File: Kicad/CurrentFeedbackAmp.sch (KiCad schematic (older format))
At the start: 97 parts, among them J1 Vin, J10 Protecc_Sup_In1, J11 Protecc_Inf_In1, J12 Protecc_Sup_In2, J13 Vdd, J14 Vcc, J15 Masa Filtros, J16 Masa Bornera Carga, J17 Bornera Carga, J18 Masa Reguladores, J2 Test_Realim_Out, J20 Masa Reguladores, J23 Masa Reguladores, J25 Masa Reguladores, J3 Masa etapa inicial, J4 Protecc_Sup_Out, J5 Protecc_Inf_Out, J8 Test_Etapa_3_Inf, J9 Test_Etapa_3_Sup, Q1 TIP42C, Q13 BC559, Q14 BC559, Q15 BC559, Q16 BC549, Q17 BC549, Q18 BC549, Q19 BC559, Q20 BC549, Q21 BC559, Q22 BC549, Q24 BD136, Q33 BD135, Q34 TIP41C, Q35 BC559, Q36 BC549, Q37 BC549, Q38 BC549, Q39 BC549, Q40 BC559, Q41 BC559, Q42 BC559, T1 BC548, T2 BC548, U1 LM7812_TO220, U2 TL082, U3 LM7912_TO220

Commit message: se actualiza la vista del simalacion
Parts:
- removed J13: Vdd, Connectors:PINTST, symbol Conn_01x01
- removed J14: Vcc, Connectors:PINTST, symbol Conn_01x01
- removed J15: Masa Filtros, Connectors:PINTST, symbol Conn_01x01
- removed J16: Masa Bornera Carga, Connectors:PINTST, symbol Conn_01x01
- removed J18, J20, J23, J25: Masa Reguladores, Connectors:PINTST, symbol Conn_01x01
- added C13, C14: 1000u, Capacitors_THT:CP_Radial_D16.0mm_P7.50mm, symbol CP
- added J6: Bornera Vcc, Connectors_Terminal_Blocks:TerminalBlock_Pheonix_MKDS1.5-2pol, symbol Screw_Terminal_01x02
- added J7: Bornera Vdd, Connectors_Terminal_Blocks:TerminalBlock_Pheonix_MKDS1.5-2pol, symbol Screw_Terminal_01x02
- C1, C2: value C -> 10n
- C10, C7: value CP -> 100u
- C11, C12, C5, C6: value C -> 220n
- C3, C4: value C -> 10p
- C8, C9: value C -> 100n
- J3: value Masa etapa inicial -> Salida masa
- R1, R2: value R -> 39
- R10, R27, R30, R5: value R -> 150
- R11, R20, R21, R6: value R -> 100
- R13, R26: value R -> 200
- R14, R25: value R -> 200; footprint Resistors_SMD:R_0805_HandSoldering -> Resistors_THT:R_Axial_DIN0204_L3.6mm_D1.6mm_P7.62mm_Horizontal
- R15: value R -> 270
- R16, R17: value R -> 50
- R18: value R -> 1k
- R19: value R -> 5.1k
- R22, R23: value R -> 100k
- R24: value R -> 10k
- R3, R8: value R -> 400
- R31.1, R31.2, R31.3, R32.1, R32.2, R32.3: value R -> 1
- R4, R9: value R -> 300
- Rref1, Rref2: symbol POT -> POT-RESCUE-CurrentFeedbackAmp
- Rref3: footprint Potentiometers:Potentiometer_Alps_RK163_Single_Vertical -> Potentiometers:Potentiometer_Trimmer_Bourns_3266Y; symbol POT -> POT-RESCUE-CurrentFeedbackAmp
- U2: footprint SMD_Packages:SOIC-8-N -> Housings_DIP:DIP-8_W7.62mm_LongPads
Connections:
- no-connect marks 1 -> 3

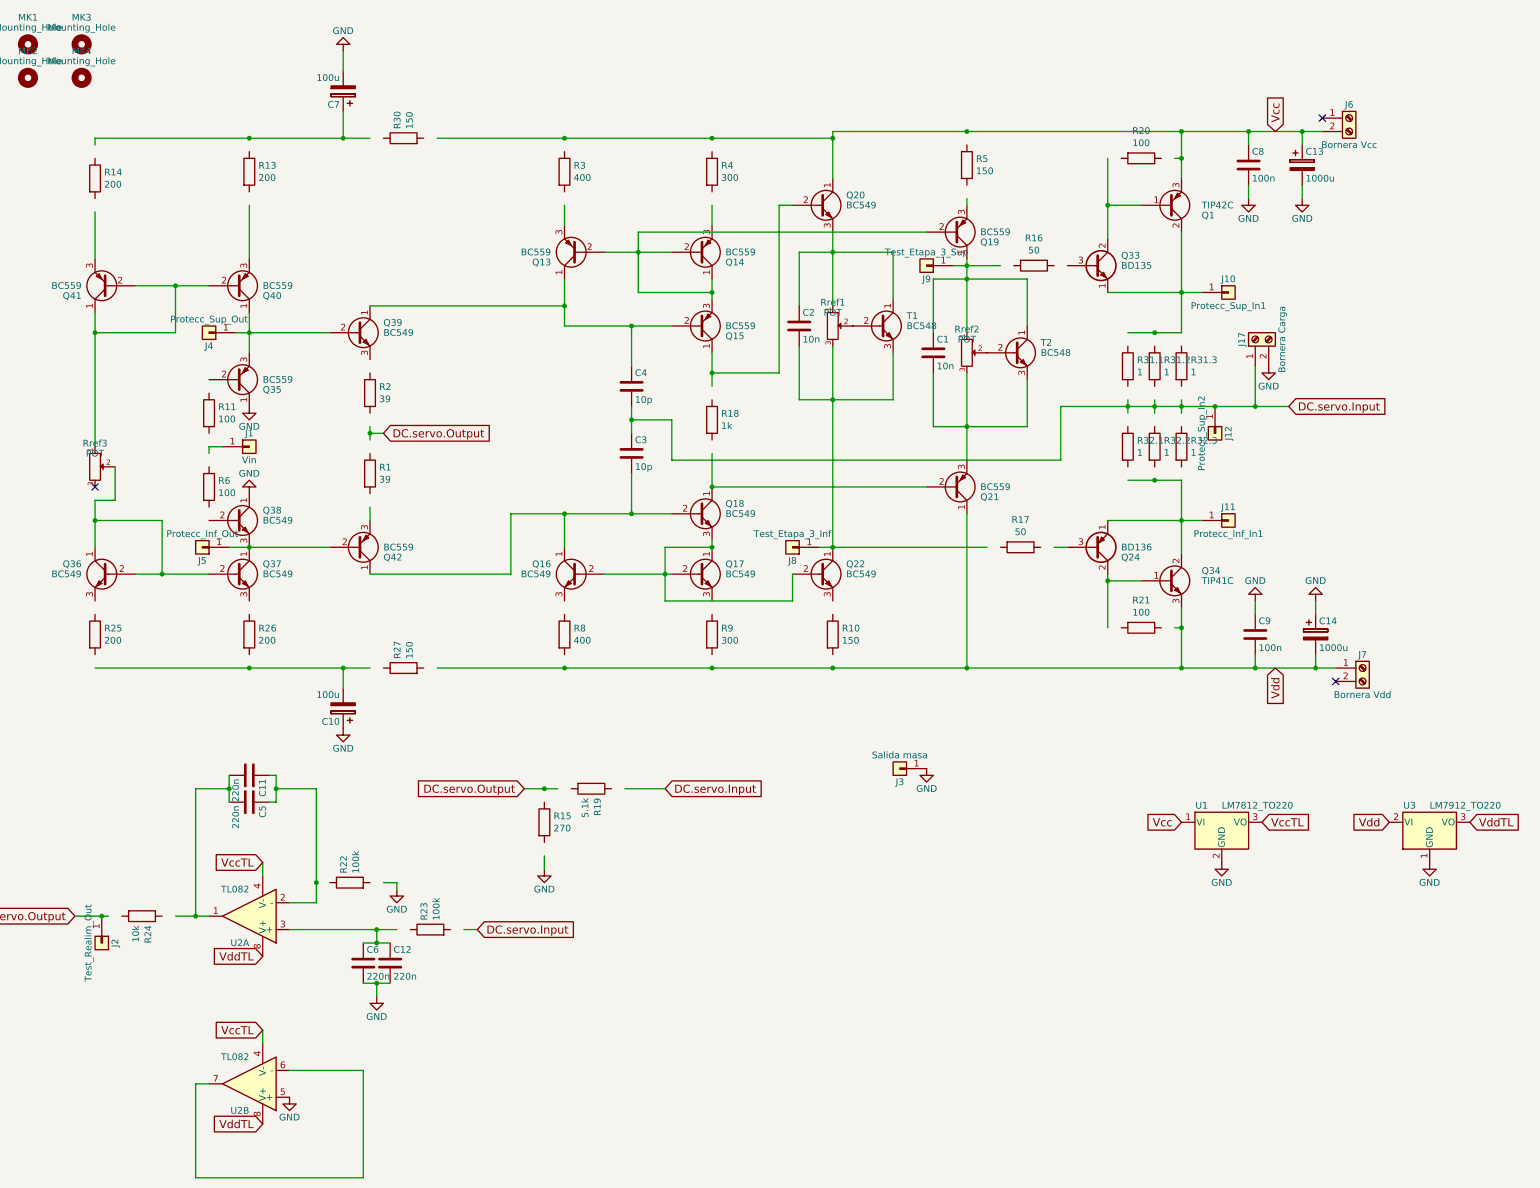
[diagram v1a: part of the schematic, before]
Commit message: ya llevamos el esquematico al KiCAD V2.0 Todavia hay que revisar el esquematico
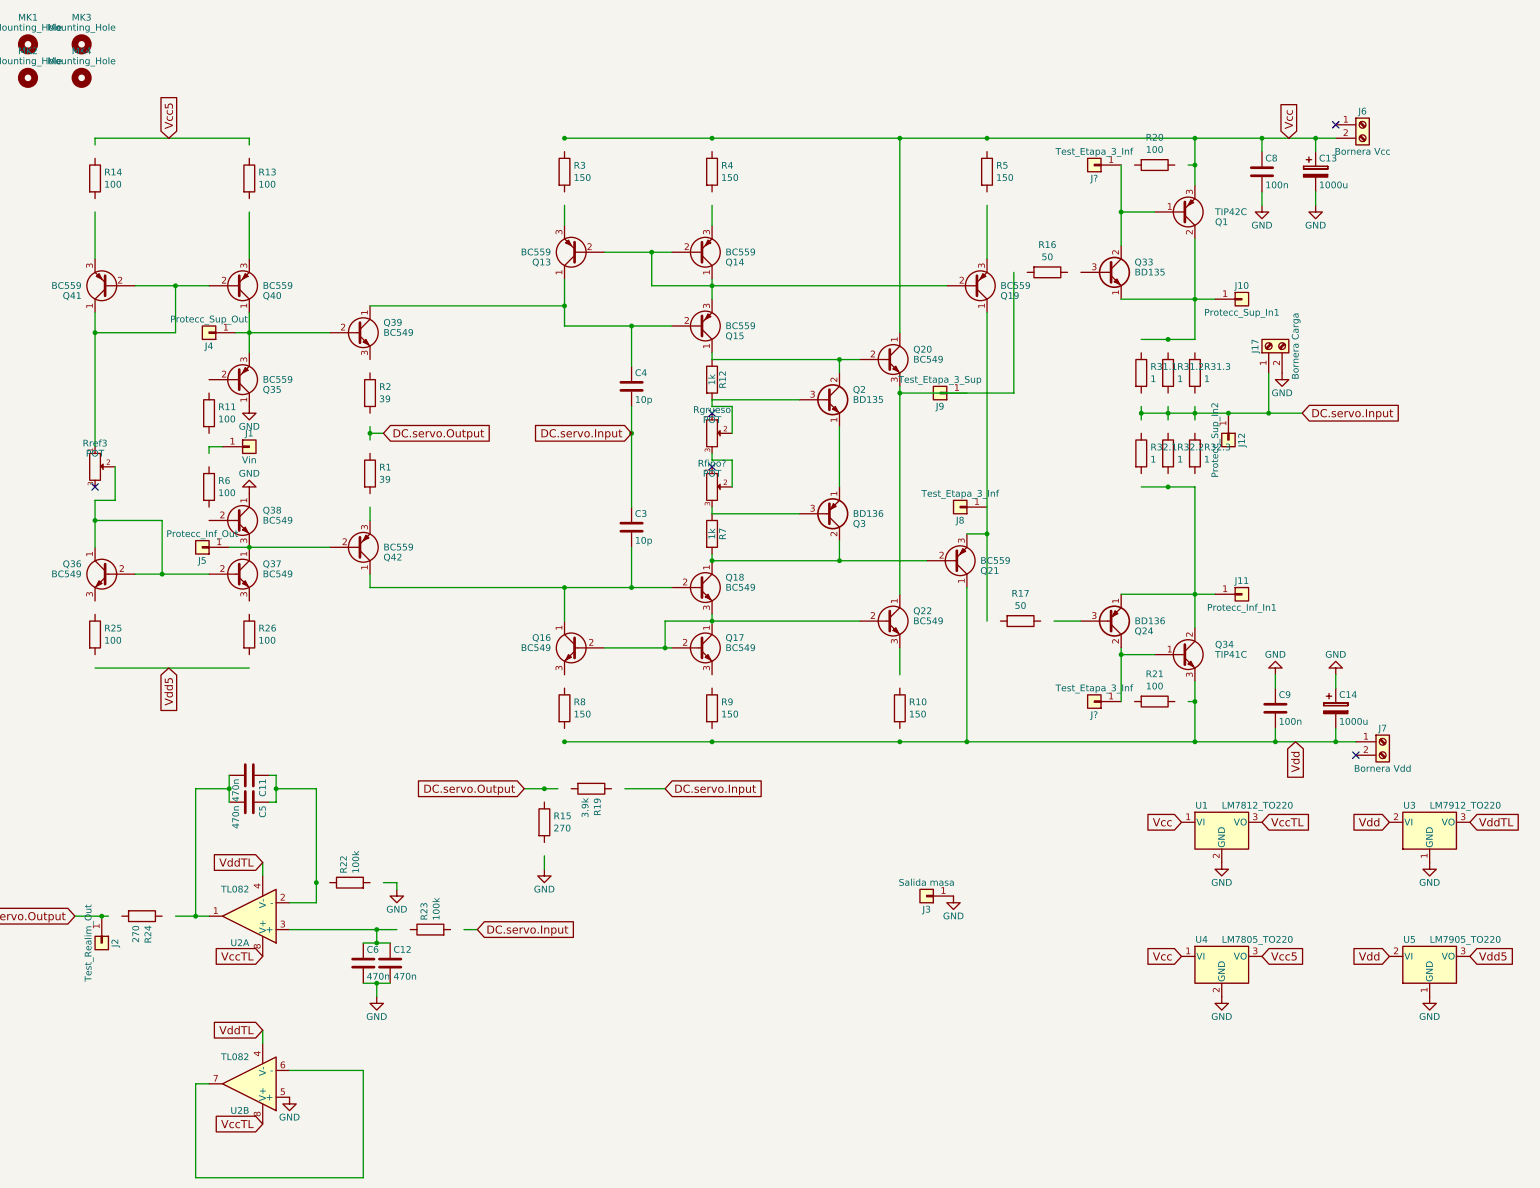
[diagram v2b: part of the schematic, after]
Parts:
- removed C1, C2: 10n, Capacitors_THT:C_Disc_D5.0mm_W2.5mm_P5.00mm, symbol C
- removed C10, C7: 100u, Capacitors_THT:CP_Radial_D8.0mm_P3.80mm, symbol CP
- removed R18: 1k, Resistors_SMD:R_0805_HandSoldering, symbol pspice:R
- removed R27, R30: 150, Resistors_SMD:R_0805_HandSoldering, symbol pspice:R
- removed Rref1, Rref2: POT, Potentiometers:Potentiometer_Trimmer_Bourns_3266Y, symbol POT-RESCUE-CurrentFeedbackAmp
- removed T1, T2: BC548, TO_SOT_Packages_THT:TO-92_Inline_Narrow_Oval, symbol BC548
- added J? (x2): Test_Etapa_3_Inf, Connectors:PINTST, symbol Conn_01x01
- added Q2: BD135, TO_SOT_Packages_THT:TO-126_Vertical, symbol BD135
- added Q3: BD136, TO_SOT_Packages_THT:TO-126_Vertical, symbol BD136
- added R12, R7: 1k, symbol R
- added Rfino?, Rgrueso: POT, Potentiometers:Potentiometer_Trimmer_Bourns_3266Y, symbol POT-RESCUE-CurrentFeedbackAmp
- added U4: LM7805_TO220, TO_SOT_Packages_THT:TO-220_Vertical, symbol LM7805_TO220
- added U5: LM7905_TO220, TO_SOT_Packages_THT:TO-220_Vertical, symbol LM7905_TO220
- C11, C12, C5, C6: value 220n -> 470n
- R13, R14, R25, R26: value 200 -> 100
- R19: value 5.1k -> 3.9k
- R24: value 10k -> 270
- R3, R8: value 400 -> 150
- R4, R9: value 300 -> 150
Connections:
- net labels added: Vcc5, Vdd5
- wire segments 140 -> 127
- no-connect marks 3 -> 5
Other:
- moved on the sheet: C13, C14, C3, C8, C9, J10, J11, J12, J17, J3, J6, J7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

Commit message: Armamos con nico el SCH en el KiCAD
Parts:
- removed J1: Vin, Connectors:PINTST, symbol Conn_01x01
- removed Q39: BC549, TO_SOT_Packages_THT:TO-92_Inline_Narrow_Oval, symbol BC549
- removed Q42: BC559, TO_SOT_Packages_THT:TO-92_Inline_Narrow_Oval, symbol BC559
- removed R1, R2: 39, Resistors_SMD:R_0805_HandSoldering, symbol pspice:R
- removed R11, R6: 100, Resistors_SMD:R_0805_HandSoldering, symbol pspice:R
- added C? (x2): 0.3p, Capacitors_THT:C_Disc_D5.0mm_W2.5mm_P5.00mm, symbol C
- added C? (x2): 100n, Capacitors_THT:C_Disc_D5.0mm_W2.5mm_P5.00mm, symbol C
- added CCOMP3, CCOMP4: 10p, Capacitors_THT:C_Disc_D5.0mm_W2.5mm_P5.00mm, symbol C
- added Q? (x9): BC559, TO_SOT_Packages_THT:TO-92_Inline_Narrow_Oval, symbol BC559
- added Q? (x9): BC549, TO_SOT_Packages_THT:TO-92_Inline_Narrow_Oval, symbol BC549
- added R? (x4): 100, Resistors_SMD:R_0805_HandSoldering, symbol pspice:R
- added R? (x4): 50, Resistors_SMD:R_0805_HandSoldering, symbol pspice:R
- added R? (x2): 5.1, symbol R
- R13, R14, R25, R26: value 100 -> 200
- R15, R24: value 270 -> 330
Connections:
- net labels added: Ireference1, Ireference2, Vin+, Vin-, Vout
- net labels removed: DC.servo.Input, DC.servo.Output
- wire segments 127 -> 216
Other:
- moved on the sheet: C11, C12, C13, C14, C3, C4, C5, C6, C8, C9, J10, J11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

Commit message: se agrega el pin de entrada, hay que ver si ya podemos empezar con el PCB
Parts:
- added J?: Entrada, Connectors:PINTST, symbol Conn_01x01
- gave numbers to parts that had none: 35
- renumbered Rgrueso to Rgrueso1
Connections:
- wire segments 216 -> 219
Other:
- moved on the sheet: U1, U4

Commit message: Conectores de tensiones de alimentacion ahora son banana y el conector de la entrada ahora es un BNC hembra
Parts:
- removed J6: Bornera Vcc, Connectors_Terminal_Blocks:TerminalBlock_Pheonix_MKDS1.5-2pol, symbol Screw_Terminal_01x02
- removed J7: Bornera Vdd, Connectors_Terminal_Blocks:TerminalBlock_Pheonix_MKDS1.5-2pol, symbol Screw_Terminal_01x02
- added J15: Salida masa2, Connectors:Banana_Jack_1Pin, symbol Conn_01x01
- added J6: Conector Vcc, Connectors_Terminal_Blocks:TerminalBlock_Pheonix_MKDS1.5-2pol, symbol Conn_01x01
- added J7: Conector Vdd, Connectors_Terminal_Blocks:TerminalBlock_Pheonix_MKDS1.5-2pol, symbol Conn_01x01
- J14: renamed from J?; footprint Connectors:PINTST -> Connectors_TE-Connectivity:BNC_Socket_TYCO-AMP_LargePads; symbol Conn_01x01 -> Conn_Coaxial
- J3: value Salida masa -> Salida masa1; footprint Connectors:PINTST -> Connectors:Banana_Jack_1Pin
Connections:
- wire segments 219 -> 225
- no-connect marks 5 -> 3
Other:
- moved on the sheet: C11, C12, C5, C6, J2, J3, R15, R19, R22, R23, R24, U2A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

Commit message: Modificado conector bornera de salida por dos banana
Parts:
- removed J17: Bornera Carga, Connectors_Terminal_Blocks:TerminalBlock_Pheonix_MKDS1.5-2pol, symbol Screw_Terminal_01x02
- added J16: Salida tierra, Connectors:Banana_Jack_1Pin, symbol Conn_01x01
- added J17: Salida senal, Connectors:Banana_Jack_1Pin, symbol Conn_01x01
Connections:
- wire segments 225 -> 226
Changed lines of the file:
@@
-$EndComp
-$Comp
-L Screw_Terminal_01x02 J17
-U 1 1 5B2D0185
-P 19400 2800
-F 0 "J17" H 19400 2900 50  0000 C CNN
-F 1 "Bornera Carga" H 19400 2600 50  0000 C CNN
-F 2 "Connectors_Terminal_Blocks:TerminalBlock_Pheonix_MKDS1.5-2pol" H 19400 2800 50  0001 C CNN
-F 3 "" H 19400 2800 50  0001 C CNN
-	1    19400 2800
-	0    -1   -1   0
 $EndComp
 $Comp
 L GND #PWR06
 U 1 1 5B2D146B
-P 19500 3000
-F 0 "#PWR06" H 19500 2750 50  0001 C CNN
-F 1 "GND" H 19500 2850 50  0000 C CNN
-F 2 "" H 19500 3000 50  0001 C CNN
-F 3 "" H 19500 3000 50  0001 C CNN
-	1    19500 3000
+P 19700 3050
+F 0 "#PWR06" H 19700 2800 50  0001 C CNN
+F 1 "GND" H 19700 2900 50  0000 C CNN
+F 2 "" H 19700 3050 50  0001 C CNN
+F 3 "" H 19700 3050 50  0001 C CNN
+	1    19700 3050
 	1    0    0    -1
 $EndComp
@@
 Wire Wire Line
 	9450 4950 9450 4850
+$Comp
+L Conn_01x01 J17
+U 1 1 5BAA4B26
+P 19400 2800
+F 0 "J17" H 19400 2900 50  0000 C CNN
+F 1 "Salida senal" H 19400 2700 50  0000 C CNN
+F 2 "Connectors:Banana_Jack_1Pin" H 19400 2800 50  0001 C CNN
+F 3 "" H 19400 2800 50  0001 C CNN
+	1    19400 2800
+	0    -1   -1   0
+$EndComp
+$Comp
+L Conn_01x01 J16
+U 1 1 5BAA51C2
+P 19700 2800
+F 0 "J16" H 19700 2900 50  0000 C CNN
+F 1 "Salida tierra" H 19700 2700 50  0000 C CNN
+F 2 "Connectors:Banana_Jack_1Pin" H 19700 2800 50  0001 C CNN
+F 3 "" H 19700 2800 50  0001 C CNN
+	1    19700 2800
+	0    -1   -1   0
+$EndComp
+Wire Wire Line
+	19700 3050 19700 3000
 $EndSCHEMATC

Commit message: Cambiados transistores de fuente de corriente por sus equivalentes SMD
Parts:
- added R32: 1k, symbol R
- Q35, Q40, Q41: value BC559 -> BC858; footprint TO_SOT_Packages_THT:TO-92_Inline_Narrow_Oval -> TO_SOT_Packages_SMD:SOT-23
- Q36, Q37, Q38: value BC549 -> BC848; footprint TO_SOT_Packages_THT:TO-92_Inline_Narrow_Oval -> TO_SOT_Packages_SMD:SOT-23
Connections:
- wire segments 226 -> 223
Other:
- moved on the sheet: Rfino1, Rgrueso1
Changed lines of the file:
@@
 P 1950 3450
 F 0 "Q35" H 2150 3525 50  0000 L CNN
-F 1 "BC559" H 2150 3450 50  0000 L CNN
-F 2 "TO_SOT_Packages_THT:TO-92_Inline_Narrow_Oval" H 2150 3375 50  0001 L CIN
+F 1 "BC858" H 2150 3450 50  0000 L CNN
+F 2 "TO_SOT_Packages_SMD:SOT-23" H 2150 3375 50  0001 L CIN
 F 3 "" H 1950 3450 50  0001 L CNN
 	1    1950 3450
@@
 P 1950 2750
 F 0 "Q40" H 2150 2825 50  0000 L CNN
-F 1 "BC559" H 2150 2750 50  0000 L CNN
-F 2 "TO_SOT_Packages_THT:TO-92_Inline_Narrow_Oval" H 2150 2675 50  0001 L CIN
+F 1 "BC858" H 2150 2750 50  0000 L CNN
+F 2 "TO_SOT_Packages_SMD:SOT-23" H 2150 2675 50  0001 L CIN
 F 3 "" H 1950 2750 50  0001 L CNN
 	1    1950 2750
@@
 P 1000 2750
 F 0 "Q41" H 1200 2825 50  0000 L CNN
-F 1 "BC559" H 1200 2750 50  0000 L CNN
-F 2 "TO_SOT_Packages_THT:TO-92_Inline_Narrow_Oval" H 1200 2675 50  0001 L CIN
+F 1 "BC858" H 1200 2750 50  0000 L CNN
+F 2 "TO_SOT_Packages_SMD:SOT-23" H 1200 2675 50  0001 L CIN
 F 3 "" H 1000 2750 50  0001 L CNN
 	1    1000 2750
@@
 P 1000 4900
 F 0 "Q36" H 1200 4975 50  0000 L CNN
-F 1 "BC549" H 1200 4900 50  0000 L CNN
-F 2 "TO_SOT_Packages_THT:TO-92_Inline_Narrow_Oval" H 1200 4825 50  0001 L CIN
+F 1 "BC848" H 1200 4900 50  0000 L CNN
+F 2 "TO_SOT_Packages_SMD:SOT-23" H 1200 4825 50  0001 L CIN
 F 3 "" H 1000 4900 50  0001 L CNN
 	1    1000 4900
@@
 P 1950 4900
 F 0 "Q37" H 2150 4975 50  0000 L CNN
-F 1 "BC549" H 2150 4900 50  0000 L CNN
-F 2 "TO_SOT_Packages_THT:TO-92_Inline_Narrow_Oval" H 2150 4825 50  0001 L CIN
+F 1 "BC848" H 2150 4900 50  0000 L CNN
+F 2 "TO_SOT_Packages_SMD:SOT-23" H 2150 4825 50  0001 L CIN
 F 3 "" H 1950 4900 50  0001 L CNN
 	1    1950 4900
@@
 P 1950 4350
 F 0 "Q38" H 2150 4425 50  0000 L CNN
-F 1 "BC549" H 2150 4350 50  0000 L CNN
-F 2 "TO_SOT_Packages_THT:TO-92_Inline_Narrow_Oval" H 2150 4275 50  0001 L CIN
+F 1 "BC848" H 2150 4350 50  0000 L CNN
+F 2 "TO_SOT_Packages_SMD:SOT-23" H 2150 4275 50  0001 L CIN
 F 3 "" H 1950 4350 50  0001 L CNN
 	1    1950 4350
@@
 L POT-RESCUE-CurrentFeedbackAmp Rfino1
 U 1 1 5B9A32E5
-P 15250 3850
-F 0 "Rfino1" V 15075 3850 50  0000 C CNN
-F 1 "POT" V 15150 3850 50  0000 C CNN
-F 2 "Potentiometers:Potentiometer_Trimmer_Bourns_3266Y" H 15250 3850 50  0001 C CNN
-F 3 "" H 15250 3850 50  0001 C CNN
-	1    15250 3850
+P 15050 3900
+F 0 "Rfino1" V 14950 4100 50  0000 C CNN
+F 1 "POT" V 15150 4000 50  0000 C CNN
+F 2 "Potentiometers:Potentiometer_Trimmer_Bourns_3266Y" H 15050 3900 50  0001 C CNN
+F 3 "" H 15050 3900 50  0001 C CNN
+	1    15050 3900
 	0    1    1    0
 $EndComp
@@
 U 1 1 5B9AC1ED
 P 15850 3200
-F 0 "Q2" H 16050 3275 50  0000 L CNN
-F 1 "BD135" H 16050 3200 50  0000 L CNN
+F 0 "Q2" H 16000 3300 50  0000 L CNN
+F 1 "BD135" H 16000 3100 50  0000 L CNN
 F 2 "TO_SOT_Packages_THT:TO-126_Vertical" H 16050 3125 50  0001 L CIN
 F 3 "" H 15850 3200 50  0001 L CNN
@@
 U 1 1 5B9AC329
 P 15850 4050
-F 0 "Q3" H 16050 4125 50  0000 L CNN
-F 1 "BD136" H 16050 4050 50  0000 L CNN
+F 0 "Q3" H 16000 4150 50  0000 L CNN
+F 1 "BD136" H 16000 3950 50  0000 L CNN
 F 2 "TO_SOT_Packages_THT:TO-126_Vertical" H 16050 3975 50  0001 L CIN
 F 3 "" H 15850 4050 50  0001 L CNN
@@
 L POT-RESCUE-CurrentFeedbackAmp Rgrueso1
 U 1 1 5B9AC6D3
-P 15250 3450
-F 0 "Rgrueso1" V 15075 3450 50  0000 C CNN
-F 1 "POT" V 15150 3450 50  0000 C CNN
-F 2 "Potentiometers:Potentiometer_Trimmer_Bourns_3266Y" H 15250 3450 50  0001 C CNN
-F 3 "" H 15250 3450 50  0001 C CNN
-	1    15250 3450
+P 15050 3200
+F 0 "Rgrueso1" V 15100 3450 50  0000 C CNN
+F 1 "POT" V 15200 3350 50  0000 C CNN
+F 2 "Potentiometers:Potentiometer_Trimmer_Bourns_3266Y" H 15050 3200 50  0001 C CNN
+F 3 "" H 15050 3200 50  0001 C CNN
+	1    15050 3200
 	0    1    1    0
 $EndComp
 Wire Wire Line
-	15250 4050 15250 4000
-Wire Wire Line
-	15400 3850 15400 3650
-Wire Wire Line
-	15400 3650 15250 3650
-Wire Wire Line
-	15250 3650 15250 3600
-Wire Wire Line
-	15400 3450 15400 3250
-Wire Wire Line
-	15400 3250 15250 3250
-Wire Wire Line
-	15250 3250 15250 3200
-NoConn ~ 15250 3700
-NoConn ~ 15250 3300
+	15250 3900 15250 4050
+NoConn ~ 15050 4050
+NoConn ~ 15050 3050
 Wire Wire Line
 	16200 2900 16200 3000
@@
 Wire Wire Line
 	15950 3850 15950 3400
-Wire Wire Line
-	15250 3200 15650 3200
 $Comp
 L R R30
@@
 Wire Wire Line
 	19700 3050 19700 3000
+$Comp
+L R R32
+U 1 1 5BAB192A
+P 15050 3550
+F 0 "R32" V 15130 3550 50  0000 C CNN
+F 1 "1k" V 15050 3550 50  0000 C CNN
+F 2 "" V 14980 3550 50  0001 C CNN
+F 3 "" H 15050 3550 50  0001 C CNN
+	1    15050 3550
+	1    0    0    -1
+$EndComp
+Wire Wire Line
+	15200 3200 15650 3200
+Connection ~ 15250 3200
+Wire Wire Line
+	15200 3900 15250 3900
+Wire Wire Line
+	15050 3750 15050 3700
+Wire Wire Line
+	15050 3400 15050 3350
 $EndSCHEMATC
